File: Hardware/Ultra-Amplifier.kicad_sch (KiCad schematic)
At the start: 61 parts, among them U11 TL071HIDBV, U12 TL071HIDBV, U13 TL071HIDBV, U18 TL071HIDBV, U19 TL071HIDBV, U20 TL071HIDBV, U21 TL071HIDBV, U7 TL071HIDBV

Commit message: Finished the VDP-board, finished up the mixer-section, removed the buffer-pins from the FPGA, and instead added external buffers for the slots, designed a marquee-block with the Ultra-MSX logo, designed the logotype, andmultiple other changes.
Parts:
- removed C21, C35: C_GRM32EC81C476KE15K, Capacitor_SMD:C_1210_3225Metric, symbol LRJ-parts:C_GRM32EC81C476KE15K
- removed C36, C37: C_GRM21BR71A106KA73K, Capacitor_SMD:C_0805_2012Metric_Pad1.18x1.45mm_HandSolder, symbol LRJ-parts:C_GRM21BR71A106KA73K
- removed C48, C49: 47pF, Capacitor_SMD:C_0603_1608Metric, symbol Device:C
- removed R114: 0R, Resistor_SMD:R_0603_1608Metric, symbol Device:R
- removed R119, R120: 100k, Resistor_SMD:R_0603_1608Metric, symbol Device:R
- removed R17: 4.7k, Resistor_SMD:R_0603_1608Metric, symbol Device:R
- removed R38, R39, R44: 22k, Resistor_SMD:R_0603_1608Metric, symbol Device:R
- removed RV1, RV2, RV3, RV4, RV5, RV6, RV7: R_Potentiometer_Dual_Separate, symbol Device:R_Potentiometer_Dual_Separate
- added C21, C35, C70, C72, C73: C_GRM21BR71A106KA73K, Capacitor_SMD:C_0805_2012Metric_Pad1.18x1.45mm_HandSolder, symbol LRJ-parts:C_GRM21BR71A106KA73K
- added C48, C49, C79, C80, C81, C82, C83, C85, C87, C89: C_CC0805JPX7R9BB104, Capacitor_SMD:C_0805_2012Metric, symbol LRJ-parts:C_CC0805JPX7R9BB104
- added C76, C77, C78: 47pF, Capacitor_SMD:C_0603_1608Metric, symbol Device:C
- added J1: Conn_RCJ-022, LRJ:CUI_RCJ-022, symbol LRJ-parts:Conn_RCJ-022
- added J2: Conn_RCJ-023, LRJ:CUI_RCJ-023, symbol LRJ-parts:Conn_RCJ-023
- added R11, R13, R14, R15, R27, R3, R4, R5, R7, R8, R9: 22k, Resistor_SMD:R_0603_1608Metric, symbol Device:R
- added R2, R6: 4.7k, Resistor_SMD:R_0603_1608Metric, symbol Device:R
- added R25: 47k, Resistor_SMD:R_0603_1608Metric, symbol Device:R
- added RV1: CAT5140ZI-50, Package_SO:TSSOP-8_3x3mm_P0.65mm, symbol LRJ-parts:CAT5140ZI-50
- added RV2, RV4: AD5144ABRUZ100, Package_SO:TSSOP-20_4.4x6.5mm_P0.65mm, symbol LRJ-parts:AD5144ABRUZ100
- added RV5, RV6: MCP4461, Package_SO:TSSOP-20_4.4x6.5mm_P0.65mm, symbol LRJ-parts:MCP4461
- added U3: TL071HIDBV, Package_TO_SOT_SMD:SOT-23-5, symbol LRJ-parts:TL071HIDBV
- R30: value 4.7k -> 22k
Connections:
- net FMA-CH1_L: now also C21.2
- net FMA-CH2_R: now also C35.2
- net FMA_L: now also R9.1, RV5.2 (P3W); no longer C57.1, U20.4 (-)
- net FMA_R: now also R11.1, RV5.19 (P2W); no longer C58.1, U21.4 (-)
- net PSG_Ch: now also RV6.9 (P1W)
- net PSG_SND: now also C70.2; no longer C43.2
- net SLT1_Ch: now also RV6.19 (P2W)
- net SLT1_SND: now also C73.2
- net SLT2_Ch: now also RV6.12 (P0W)
- net SLT2_SND: now also C72.2
- net at R33.2: now also RV2.3 (A1)
- net at C44.2, U12.1 (OUT): now also RV4.4 (W1), RV5.1 (P3A)
- net at R30.2: now also RV2.10 (A2)
- net at R12.1: now also C35.1
- net at C45.1, R12.2, U13.4 (-): now also R5.1; no longer R36.1
- net at C47.2: now also U18.1 (OUT), RV4.14 (W4), RV5.11 (P0A); no longer U11.1 (OUT)
- net at C57.2, C61.1, U20.1 (OUT): now also RV6.2 (P3W)
- net at C45.2, U13.1 (OUT): now also RV4.11 (W2), RV5.20 (P2A)
- net -12VA: now reaches U13.5 (V+)
- net -12VA: now also C50.1, C53.1, C60.1, U11.5 (V+), U12.5 (V+), U18.5 (V+), U19.5 (V+), U20.5 (V+), U21.5 (V+), U7.5 (V+), C48.1, C49.1, C79.1, C80.1, C81.1, C87.1, U3.5 (V+)
- net at R115.1, R116.1, R117.1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: now also R14.1, R15.2
- net at C46.2: now also RV4.7 (W3), RV5.10 (P1A), U3.1 (OUT); no longer U7.1 (OUT)
- net at R31.1, U18.4 (-): now also C47.1, R7.1
- net at R31.2: now also C43.1; no longer C38.1
- net at R32.1, U19.4 (-): now also R30.1, C77.1
- net at U19.1 (OUT): now also C77.2, RV2.11 (W2), RV6.10 (P1A)
- net +12VA: now reaches U19.2 (V-)
- net +12VA: now also C51.1, C52.1, C54.1, C55.1, C65.1, U11.2 (V-), U12.2 (V-), U13.2 (V-), U18.2 (V-), U20.2 (V-), U21.2 (V-), U7.2 (V-), C82.1, C83.1, C85.1, C89.1, U3.2 (V-)
- net at C58.2, C64.1, U21.1 (OUT): now also RV1.5 (RW)
- net at R10.1: now also C21.1
- net at C44.1, R10.2, U12.4 (-): now also R4.1; no longer R33.1
- net at R37.2: now also RV6.16 (A1)
- net at R32.2: now also C70.1; no longer C43.1
- net at R36.2: now also RV5.4 (A0/HVC)
- removed net +12V: C53.1, C54.1, C55.1, C65.1, U12.5 (V+), U18.5 (V+), U19.5 (V+), U20.5 (V+)
- removed net -12V: C50.1, C51.1, C52.1, C60.1, U11.2 (V-), U13.2 (V-), U21.2 (V-), U7.2 (V-)
- net GND renamed GNDA
- net GNDA: now also R36.1, R37.1, C48.2, C49.2, C79.2, C80.2, C81.2, C82.2, C83.2, C85.2, C87.2, C89.2, J1.1A (IN1), J1.1B (IN1), J2.1A (IN1), J2.1B (IN1), RV5.13 (P0B), RV5.18 (P2B), RV5.3 (P3B), RV5.8 (P1B), RV6.13 (P0B), RV6.18 (P2B), RV6.8 (P1B), U3.3 (+)
- net SLT3_SND renamed SLT3_SND_R
- net SLT3_SND_R: now also J2.2 (IN2)
- new net: C76.1, R27.1, R6.1, U7.4 (-)
- new net: C72.1, R6.2
- new net: C46.1, R2.1, R3.1, U3.4 (-)
- new net: C58.1, R11.2, R13.2, R15.1, RV1.7 (RH), U21.4 (-)
- new net: C57.1, R14.2, R8.2, R9.2, RV6.1 (P3A), U20.4 (-)
- new net: R3.2, RV4.6 (A3)
- new net: C73.1, R25.1
- new net: C78.1, R25.2, R33.1, U11.4 (-)
- new net: R7.2, RV4.13 (A4)
- new net: C78.2, RV2.4 (W1), RV6.20 (P2A), U11.1 (OUT)
- new net: C76.2, RV2.7 (W3), RV6.11 (P0A), U7.1 (OUT)
- new net: C38.1, R2.2
- new net: R5.2, RV4.10 (A2)
- new net: R27.2, RV2.6 (A3)
- new net: R4.2, RV4.3 (A1)
- new net I2C_AD1: RV5.16 (A1)
- new net I2C_AD2: RV4.20 (ADDR)
- new net I2C_AD3: RV6.4 (A0/HVC)
- new net I2C_SCL: RV1.2 (SCL), RV4.18 (SCL), RV5.5 (SCL), RV6.5 (SCL)
- new net I2C_SDA: RV1.3 (SDA), RV4.19 (SDA), RV5.6 (SDA), RV6.6 (SDA)
- new net I2C_~{WP}: RV1.1 (~{WP}), RV5.14 (~{WP})
- new net SL3-B: RV4.15 (B4), RV4.8 (B3)
- new net SLP_B: RV2.12 (B2), RV2.8 (B3)
- new net SLT3_L: R8.1, RV5.12 (P0W)
- new net SLT3_R: R13.1, RV5.9 (P1W)
- new net SLT3_SND_L: C43.2, J1.2 (IN2)
- new net SUM_B: RV1.6 (RL), RV6.3 (P3B)
- new net YAM-B: RV2.5 (B1), RV4.12 (B2), RV4.5 (B1)
- no-connect marks 16 -> 4
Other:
- note added: "External input, if Audio-source has external output."
- note added: "Get a combined converter-chip, that can do both JTAG and SPI to GPIO? Microcontroller Specs: 25+ MHz USART/UART (2 pins) USB (4 pins) GPIO (8 pins) SPI (4 pins) I2C (4 pins) 6+8+8 = 22 IO example: M258KE3AE With an FPGA: AT40K10-2AJC"
- note added: "How to build an Audio mixer: https://www.circuitlib.com/index.php/tutorials/product/39-how-to-build-an-audio-mixer -- How to inject Mono into Stereo-output; Build a Virtual Earth Summing Amp "Make sure you use linear taper pots for the pans and audio taper pots for the faders." https://electronics.stackexchange.com/questions/236764/diy-mixer-use-diodes-to-prevent-input-potentiometers-influencing-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"
- note added: "Input-Module for Slot 3 Audio"
- note added: "Input-Module for Yamaha Audio"
- note added: "Inverting Pre-Amplifier for PSG Channel"
- note added: "Inverting Pre-Amplifier for Slot 1 Audio"
- note added: "Inverting Pre-Amplifier for Slot 2 Audio"
- note added: "Inverting Pre-Amplifier for Slot 3 Left"
- note added: "Inverting Pre-Amplifier for Slot 3 Right"
- note added: "Inverting Pre-Amplifier for ym Left"
- note added: "Inverting Pre-Amplifier for ym Right"
- note added: "Set MC-pots as close as possible to 22K"
- note added: "Volume"
- note removed: "Pre-Amplifier for FMA Channel 1"
- note removed: "Pre-Amplifier for FMA Channel 2"
- note removed: "Pre-Amplifier for PSG Channel"
- note removed: "Pre-Amplifier for Slot 1 Audio"
- note removed: "Pre-Amplifier for Slot 2 Audio"
- note removed: "Pre-Amplifier for Slot 3 Audio"
- title: Audio Amplifiers -> ULTRA-MSX
- moved on the sheet: C56, C57, C58, C60, C61, C64, C65, R10, R115, R116, R117, R118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

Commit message: Added SD-card slot, made basic 3d-model for sd-card slot, connected it up in the schematic, and numerous other tweaks.
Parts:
- removed R36, R37: 22k, Resistor_SMD:R_0603_1608Metric, symbol Device:R
- removed RV1: CAT5140ZI-50, Package_SO:TSSOP-8_3x3mm_P0.65mm, symbol LRJ-parts:CAT5140ZI-50
- added unit 1 of RV3
- added unit 5 of RV3
- C44, C45, C46, C47, C76, C77, C78: value 47pF -> C
- C57, C58: value 22pF -> C
- C61, C64: value 4.7uF -> C
- R10, R12, R25: value 47k -> R
- R11, R13, R14, R15, R27, R3, R30, R33, R4, R5, R7, R8, R9: value 22k -> R
- R115, R116, R117: value 0R -> R
- R118: value 20k -> R
- R121, R122: value 47R -> R
- R2, R31, R6: value 4.7k -> R
- R32: value 2.2k -> R
- RV1: renamed from RV4; Tolerance (none) -> ±8%
- RV2: renamed from RV5; value MCP4461 -> AD5144ABRUZ100; symbol LRJ-parts:MCP4461 -> LRJ-parts:AD5144ABRUZ100; MPN MCP4461-503E/ST -> AD5144ABRUZ100; Manufacturer Microchip Technology -> Analog Devices Inc.; Tolerance (none) -> ±8%
- RV3: renamed from RV2; Tolerance (none) -> ±8%
- RV4: renamed from RV6; value MCP4461 -> AD5144ABRUZ100; symbol LRJ-parts:MCP4461 -> LRJ-parts:AD5144ABRUZ100; MPN MCP4461-503E/ST -> AD5144ABRUZ100; Manufacturer Microchip Technology -> Analog Devices Inc.; Tolerance (none) -> ±8%
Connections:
- net FMA_L: now also RV2.14 (W4); no longer RV2.2 (P3W)
- net FMA_R: now also RV2.7 (W3); no longer RV2.19 (P2W)
- net GNDA: now also RV2.12 (B2), RV2.15 (B4), RV2.5 (B1), RV2.8 (B3), RV4.12 (B2), RV4.5 (B1), RV4.8 (B3); no longer RV2.13 (P0B), RV2.18 (P2B), RV2.3 (P3B), RV2.8 (P1B), RV4.13 (P0B), RV4.18 (P2B), RV4.8 (P1B)
- net I2C_AD1: now also RV1.20 (ADDR); no longer RV2.16 (A1)
- net I2C_AD2: now also RV2.20 (ADDR); no longer RV1.20 (ADDR)
- net I2C_AD3: now also RV3.20 (ADDR); no longer RV4.4 (A0/HVC)
- net I2C_SCL: now also RV2.18 (SCL), RV4.18 (SCL), RV3.18 (SCL); no longer RV2.5 (SCL), RV4.5 (SCL)
- net I2C_SDA: now also RV2.19 (SDA), RV4.19 (SDA), RV3.19 (SDA); no longer RV2.6 (SDA), RV4.6 (SDA)
- net PSG_Ch: now also RV4.11 (W2); no longer RV4.9 (P1W)
- net SLT1_Ch: now also RV4.7 (W3); no longer RV4.19 (P2W)
- net SLT2_Ch: now also RV4.4 (W1); no longer RV4.12 (P0W)
- net SLT3_L: now also RV2.4 (W1); no longer RV2.12 (P0W)
- net SLT3_R: now also RV2.11 (W2); no longer RV2.9 (P1W)
- net SUM_B: now also RV4.15 (B4), RV3.15 (B4); no longer RV4.3 (P3B)
- net at C58.1, R11.2, R13.2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: now also RV3.13 (A4)
- net at C44.2, RV1.4 (W1), U12.1 (OUT): now also RV2.13 (A4); no longer RV2.1 (P3A)
- net at C57.2, C61.1, U20.1 (OUT): now also RV4.14 (W4); no longer RV4.2 (P3W)
- net at C57.1, R14.2, R8.2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: now also RV4.13 (A4); no longer RV4.1 (P3A)
- net at C45.2, RV1.11 (W2), U13.1 (OUT): now also RV2.6 (A3); no longer RV2.20 (P2A)
- net at C47.2, RV1.14 (W4), U18.1 (OUT): now also RV2.3 (A1); no longer RV2.11 (P0A)
- net at C78.2, RV3.4 (W1), U11.1 (OUT): now also RV4.6 (A3); no longer RV4.20 (P2A)
- net at C58.2, C64.1, U21.1 (OUT): now also RV3.14 (W4)
- net at C76.2, RV3.7 (W3), U7.1 (OUT): now also RV4.3 (A1); no longer RV4.11 (P0A)
- net ~{AUD_INT}: now reaches RV1.1 (~{RESET})
- net ~{AUD_INT}: now also RV2.1 (~{RESET}), RV4.1 (~{RESET}), RV3.1 (~{RESET})
- removed net I2C_~{WP}: RV2.14 (~{WP})
- new net I2C_AD4: RV4.20 (ADDR)
- no-connect marks 4 -> 0
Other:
- note added: "Mono Injection"
- note added: "Set to 22K"
- note removed: "Set MC-pots as close as possible to 22K"
- moved on the sheet: C21, C35, C38, C43, C44, C45, C46, C47, C48, C49, C50, C51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

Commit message: Multiple redesigns of the IO-shield. Replaced FPGA with lower pin-count AT10K, since the higher pin-count one is now obsolete.
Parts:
- C48, C49, C50, C51, C52, C53, C54, C55, C60, C65, C79, C80, C81, C82, C83, C85, C87, C89: Price €0,14 -> (none)

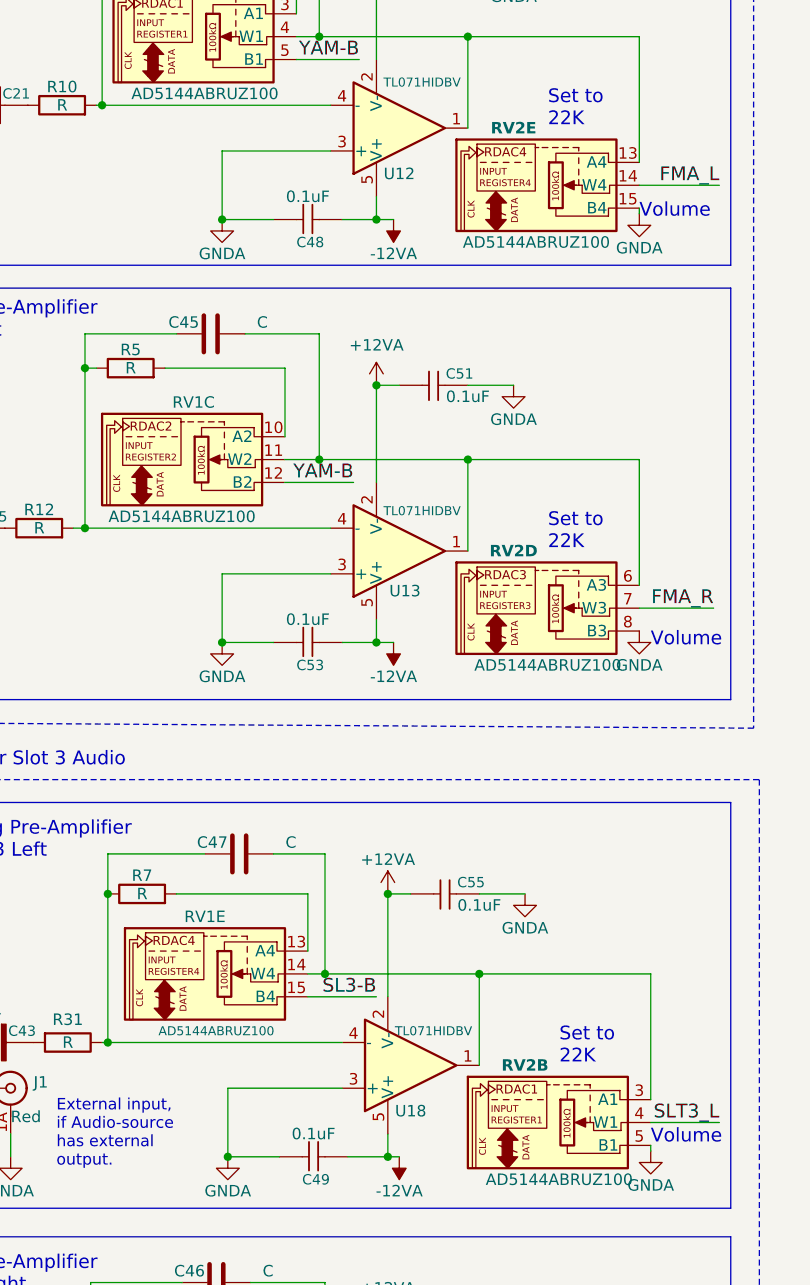
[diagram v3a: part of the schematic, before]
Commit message: Added cooler and CPU-mount footprints, as well as Indication LEDs.
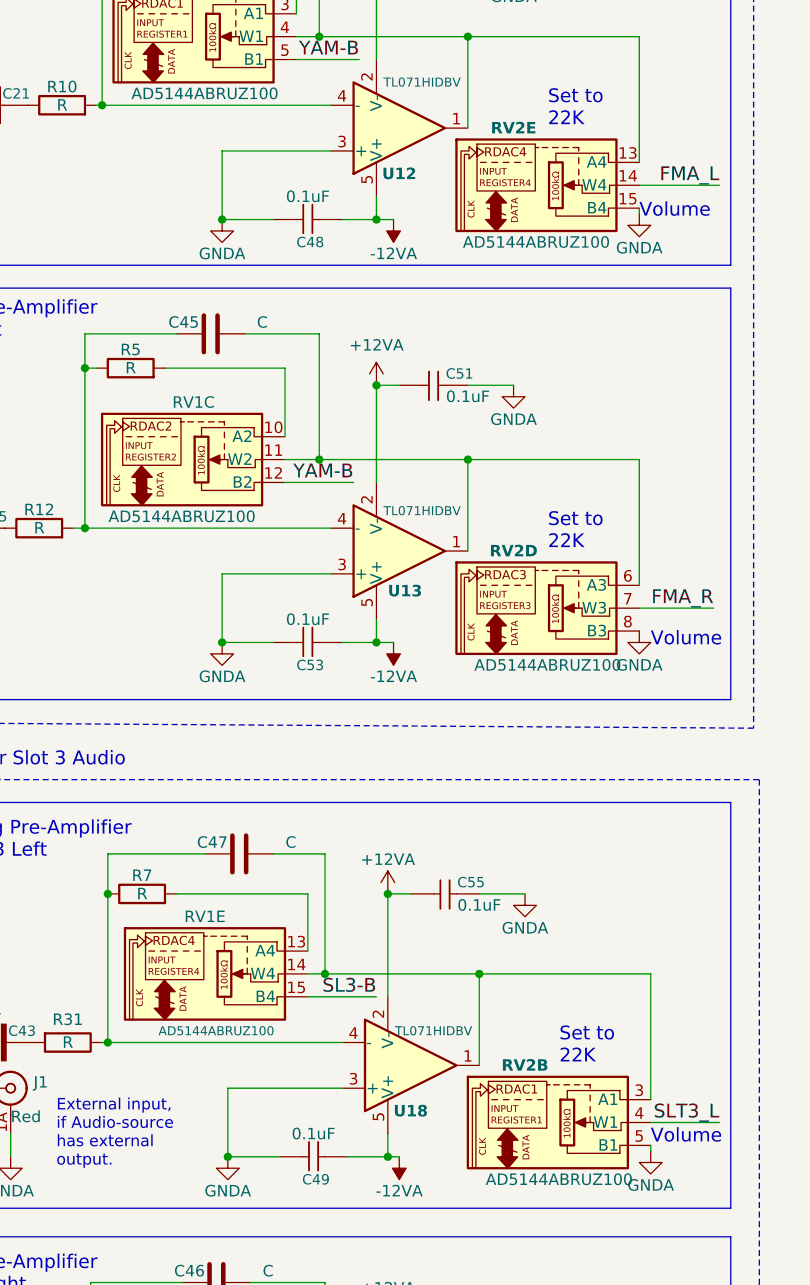
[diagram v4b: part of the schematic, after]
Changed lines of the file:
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@@
   (symbol (lib_id "LRJ-parts:TL071HIDBV") (at 77.47 130.81 0) (mirror x) (unit 1)
     (in_bom yes) (on_board yes)
-    (property "Reference" "U13" (id 0) (at 78.105 135.255 0))
+    (property "Reference" "U13" (id 0) (at 78.105 135.255 0)
+      (effects (font (size 1.27 1.27) bold))
+    )
     (property "Value" "TL071HIDBV" (id 1) (at 80.01 126.365 0)
       (effects (font (size 1 1)))
@@
   (symbol (lib_id "LRJ-parts:TL071HIDBV") (at 77.47 83.82 0) (mirror x) (unit 1)
     (in_bom yes) (on_board yes)
-    (property "Reference" "U12" (id 0) (at 77.47 88.9 0))
+    (property "Reference" "U12" (id 0) (at 77.47 88.9 0)
+      (effects (font (size 1.27 1.27) bold))
+    )
     (property "Value" "TL071HIDBV" (id 1) (at 80.01 78.74 0)
       (effects (font (size 1 1)))
@@
   (symbol (lib_id "LRJ-parts:TL071HIDBV") (at 78.74 187.96 0) (mirror x) (unit 1)
     (in_bom yes) (on_board yes)
-    (property "Reference" "U18" (id 0) (at 78.74 193.04 0))
+    (property "Reference" "U18" (id 0) (at 78.74 193.04 0)
+      (effects (font (size 1.27 1.27) bold))
+    )
     (property "Value" "TL071HIDBV" (id 1) (at 81.28 184.15 0)
       (effects (font (size 1 1)))

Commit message: Started fixing many small issues.
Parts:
- added C109, C110: C_GRM21BR71A106KA73K, Capacitor_SMD:C_0805_2012Metric_Pad1.18x1.45mm_HandSolder, symbol LRJ-parts:C_GRM21BR71A106KA73K
- added C111, C112: C, Capacitor_SMD:C_0603_1608Metric, symbol Device:C
- added C113, C114, C115, C116: C_CC0805JPX7R9BB104, Capacitor_SMD:C_0805_2012Metric, symbol LRJ-parts:C_CC0805JPX7R9BB104
- added R24, R56, R57, R58: R, Resistor_SMD:R_0603_1608Metric, symbol Device:R
- added RV5: AD5144ABRUZ100, Package_SO:TSSOP-20_4.4x6.5mm_P0.65mm, symbol LRJ-parts:AD5144ABRUZ100
- added U17, U22: TL071HIDBV, Package_TO_SOT_SMD:SOT-23-5, symbol LRJ-parts:TL071HIDBV
- renumbered U3 to U16
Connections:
- net +12VA: now also C115.1, C116.1, U17.2 (V-), U22.2 (V-)
- net -12VA: now also C113.1, C114.1, U17.5 (V+), U22.5 (V+)
- net FMA_L: now also RV1.11 (W2); no longer RV2.14 (W4)
- net FMA_R: now also RV1.14 (W4); no longer RV2.7 (W3)
- net I2C_SCL: now also RV5.18 (SCL)
- net I2C_SDA: now also RV5.19 (SDA)
- net PSG_Ch: now also RV3.14 (W4); no longer RV4.11 (W2)
- net SL3-B: now also RV2.5 (B1), RV2.8 (B3), RV4.8 (B3), RV5.5 (B1); no longer RV1.15 (B4), RV1.8 (B3)
- net SLP_B: now also RV3.5 (B1); no longer RV3.12 (B2)
- net SLT1_Ch: now also RV4.11 (W2); no longer RV4.7 (W3)
- net SLT2_Ch: now also RV3.11 (W2); no longer RV4.4 (W1)
- net SLT3_L: now also RV2.11 (W2); no longer RV2.4 (W1)
- net SLT3_R: now also RV2.14 (W4); no longer RV2.11 (W2)
- net SUM_B: now also RV5.15 (B4), RV5.8 (B3); no longer RV3.15 (B4), RV4.15 (B4)
- net YAM-B: now also RV1.8 (B3), RV4.5 (B1); no longer RV1.12 (B2), RV3.5 (B1)
- net ~{AUD_INT}: now also RV5.1 (~{RESET})
- net at R30.2: now also RV3.6 (A3); no longer RV3.10 (A2)
- net at C46.2, U16.1 (OUT): now also RV2.13 (A4), RV2.7 (W3); no longer RV1.7 (W3), RV2.10 (A2)
- net at C58.1, R11.2, R13.2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: now also RV5.13 (A4); no longer RV3.13 (A4)
- net at C44.2, RV1.4 (W1), U12.1 (OUT): now also RV1.10 (A2); no longer RV2.13 (A4)
- net at C77.2, U19.1 (OUT): now also RV3.13 (A4), RV3.7 (W3); no longer RV3.11 (W2), RV4.10 (A2)
- net at C57.2, C61.1, U20.1 (OUT): now also RV5.7 (W3); no longer RV4.14 (W4)
- net at C57.1, R14.2, R8.2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: now also RV5.6 (A3); no longer RV4.13 (A4)
- net at C45.2, U13.1 (OUT): now also RV1.13 (A4), RV1.7 (W3); no longer RV1.11 (W2), RV2.6 (A3)
- net at RV1.6 (A3): now also R5.2; no longer R3.2
- net at R7.2: now also RV2.3 (A1); no longer RV1.13 (A4)
- net at C47.2, U18.1 (OUT): now also RV2.10 (A2), RV2.4 (W1); no longer RV1.14 (W4), RV2.3 (A1)
- net at C78.2, U11.1 (OUT): now also RV4.10 (A2), RV4.4 (W1); no longer RV3.4 (W1), RV4.6 (A3)
- net at C58.2, C64.1, U21.1 (OUT): now also RV5.14 (W4); no longer RV3.14 (W4)
- net at C76.2, U7.1 (OUT): now also RV3.10 (A2), RV3.4 (W1); no longer RV3.7 (W3), RV4.3 (A1)
- net at R27.2: now also RV3.3 (A1); no longer RV3.6 (A3)
- net at R33.2: now also RV4.3 (A1); no longer RV3.3 (A1)
- net GNDA renamed GND
- net GND: now also RV1.12 (B2), RV1.15 (B4), RV3.12 (B2), RV3.15 (B4), RV4.15 (B4), C113.2, C114.2, C115.2, C116.2, RV5.12 (B2), U17.3 (+), U22.3 (+); no longer RV2.5 (B1), RV2.8 (B3), RV4.5 (B1), RV4.8 (B3)
- new net: C110.1, R56.2
- new net: C111.2, RV5.10 (A2), RV5.4 (W1), U22.1 (OUT)
- new net: C111.1, R24.1, R57.1, U22.4 (-)
- new net: R57.2, RV5.3 (A1)
- new net: R3.2, RV2.6 (A3)
- new net: C112.2, RV4.13 (A4), RV4.7 (W3), U17.1 (OUT)
- new net: C112.1, R56.1, R58.1, U17.4 (-)
- new net: C109.1, R24.2
- new net: R58.2, RV4.6 (A3)
- new net I2C_AD5: RV5.20 (ADDR)
- new net WAVE_L: C110.2, RV4.14 (W4)
- new net WAVE_R: C109.2, RV5.11 (W2)
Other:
- note added: "Input-Module for Wave-table Audio"
- note added: "Inverting Pre-Amplifier for Wave Left"
- note added: "Inverting Pre-Amplifier for Wave Right"
- moved on the sheet: C21, C35, C38, C43, C44, C45, C46, C47, C48, C49, C50, C51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
